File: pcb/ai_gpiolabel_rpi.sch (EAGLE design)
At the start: 3 parts

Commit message: updating
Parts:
- renumbered U$3 to LABEL
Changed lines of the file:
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@@
 <grid distance="50" unitdist="mil" unit="mil" style="lines" multiple="1" display="yes" altdistance="0.01" altunitdist="inch" altunit="inch"/>
 <layers>
-<layer number="1" name="Top" color="4" fill="1" visible="yes" active="no"/>
-<layer number="16" name="Bottom" color="1" fill="1" visible="yes" active="no"/>
-<layer number="17" name="Pads" color="2" fill="1" visible="yes" active="no"/>
-<layer number="18" name="Vias" color="2" fill="1" visible="yes" active="no"/>
-<layer number="19" name="Unrouted" color="6" fill="1" visible="yes" active="no"/>
-<layer number="20" name="Dimension" color="15" fill="1" visible="yes" active="no"/>
-<layer number="21" name="tPlace" color="7" fill="1" visible="yes" active="no"/>
-<layer number="22" name="bPlace" color="7" fill="1" visible="yes" active="no"/>
-<layer number="23" name="tOrigins" color="15" fill="1" visible="yes" active="no"/>
-<layer number="24" name="bOrigins" color="15" fill="1" visible="yes" active="no"/>
-<layer number="25" name="tNames" color="7" fill="1" visible="yes" active="no"/>
-<layer number="26" name="bNames" color="7" fill="1" visible="yes" active="no"/>
-<layer number="27" name="tValues" color="7" fill="1" visible="yes" active="no"/>
-<layer number="28" name="bValues" color="7" fill="1" visible="yes" active="no"/>
+<layer number="1" name="Top" color="4" fill="1" visible="no" active="no"/>
+<layer number="16" name="Bottom" color="1" fill="1" visible="no" active="no"/>
+<layer number="17" name="Pads" color="2" fill="1" visible="no" active="no"/>
+<layer number="18" name="Vias" color="2" fill="1" visible="no" active="no"/>
+<layer number="19" name="Unrouted" color="6" fill="1" visible="no" active="no"/>
+<layer number="20" name="Dimension" color="15" fill="1" visible="no" active="no"/>
+<layer number="21" name="tPlace" color="7" fill="1" visible="no" active="no"/>
+<layer number="22" name="bPlace" color="7" fill="1" visible="no" active="no"/>
+<layer number="23" name="tOrigins" color="15" fill="1" visible="no" active="no"/>
+<layer number="24" name="bOrigins" color="15" fill="1" visible="no" active="no"/>
+<layer number="25" name="tNames" color="7" fill="1" visible="no" active="no"/>
+<layer number="26" name="bNames" color="7" fill="1" visible="no" active="no"/>
+<layer number="27" name="tValues" color="7" fill="1" visible="no" active="no"/>
+<layer number="28" name="bValues" color="7" fill="1" visible="no" active="no"/>
 <layer number="29" name="tStop" color="7" fill="3" visible="no" active="no"/>
 <layer number="30" name="bStop" color="7" fill="6" visible="no" active="no"/>
@@
 <layer number="35" name="tGlue" color="7" fill="4" visible="no" active="no"/>
 <layer number="36" name="bGlue" color="7" fill="5" visible="no" active="no"/>
-<layer number="37" name="tTest" color="7" fill="1" visible="yes" active="no"/>
-<layer number="38" name="bTest" color="7" fill="1" visible="yes" active="no"/>
+<layer number="37" name="tTest" color="7" fill="1" visible="no" active="no"/>
+<layer number="38" name="bTest" color="7" fill="1" visible="no" active="no"/>
 <layer number="39" name="tKeepout" color="4" fill="11" visible="no" active="no"/>
 <layer number="40" name="bKeepout" color="1" fill="11" visible="no" active="no"/>
@@
 <layer number="44" name="Drills" color="7" fill="1" visible="no" active="no"/>
 <layer number="45" name="Holes" color="7" fill="1" visible="no" active="no"/>
-<layer number="46" name="Milling" color="3" fill="1" visible="yes" active="no"/>
-<layer number="47" name="Measures" color="7" fill="1" visible="yes" active="no"/>
-<layer number="48" name="Document" color="7" fill="1" visible="yes" active="no"/>
-<layer number="49" name="Reference" color="7" fill="1" visible="yes" active="no"/>
-<layer number="50" name="dxf" color="7" fill="1" visible="yes" active="no"/>
-<layer number="51" name="tDocu" color="7" fill="1" visible="yes" active="no"/>
-<layer number="52" name="bDocu" color="7" fill="1" visible="yes" active="no"/>
-<layer number="53" name="tGND_GNDA" color="7" fill="9" visible="yes" active="no"/>
-<layer number="54" name="bGND_GNDA" color="1" fill="9" visible="yes" active="no"/>
-<layer number="56" name="wert" color="7" fill="1" visible="yes" active="no"/>
-<layer number="57" name="tCAD" color="7" fill="1" visible="yes" active="no"/>
+<layer number="46" name="Milling" color="3" fill="1" visible="no" active="no"/>
+<layer number="47" name="Measures" color="7" fill="1" visible="no" active="no"/>
+<layer number="48" name="Document" color="7" fill="1" visible="no" active="no"/>
+<layer number="49" name="Reference" color="7" fill="1" visible="no" active="no"/>
+<layer number="50" name="dxf" color="7" fill="1" visible="no" active="no"/>
+<layer number="51" name="tDocu" color="7" fill="1" visible="no" active="no"/>
+<layer number="52" name="bDocu" color="7" fill="1" visible="no" active="no"/>
+<layer number="53" name="tGND_GNDA" color="7" fill="9" visible="no" active="no"/>
+<layer number="54" name="bGND_GNDA" color="1" fill="9" visible="no" active="no"/>
+<layer number="56" name="wert" color="7" fill="1" visible="no" active="no"/>
+<layer number="57" name="tCAD" color="7" fill="1" visible="no" active="no"/>
 <layer number="90" name="Modules" color="5" fill="1" visible="yes" active="yes"/>
 <layer number="91" name="Nets" color="2" fill="1" visible="yes" active="yes"/>
@@
 <layer number="97" name="Info" color="7" fill="1" visible="yes" active="yes"/>
 <layer number="98" name="Guide" color="6" fill="1" visible="yes" active="yes"/>
+<layer number="99" name="SpiceOrder" color="7" fill="1" visible="no" active="no"/>
 <layer number="100" name="Muster" color="7" fill="1" visible="no" active="no"/>
 <layer number="101" name="Patch_Top" color="12" fill="4" visible="no" active="yes"/>
@@
 </part>
 <part name="U$2" library="Ai_Miscellany" deviceset="AI-LOGO" device="XS"/>
-<part name="U$3" library="Ai_Connectors" deviceset="2X20-RPI" device="-NOFIRST" value="2X20-RPI-NOFIRST"/>
+<part name="LABEL" library="Ai_Connectors" deviceset="2X20-RPI" device="-NOFIRST" value="2X20-RPI-NOFIRST"/>
 <part name="U$4" library="Ai_Miscellany" deviceset="AI-LOGO" device="XS"/>
 </parts>
@@
 <instances>
 <instance part="FRAME1" gate="G$1" x="0" y="0"/>
-<instance part="FRAME1" gate="G$2" x="147.32" y="0"/>
-<instance part="U$2" gate="G$1" x="134.62" y="13.97"/>
-<instance part="U$3" gate="G$1" x="123.19" y="95.25"/>
-<instance part="U$4" gate="G$1" x="134.62" y="13.97"/>
+<instance part="FRAME1" gate="G$2" x="154.94" y="3.81"/>
+<instance part="U$2" gate="G$1" x="144.78" y="17.78"/>
+<instance part="LABEL" gate="G$1" x="123.19" y="95.25"/>
+<instance part="U$4" gate="G$1" x="144.78" y="16.51"/>
 </instances>
 <busses>

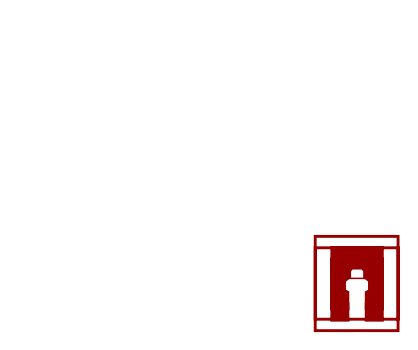
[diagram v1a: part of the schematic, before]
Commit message: Added README, LICENSE, and panelized
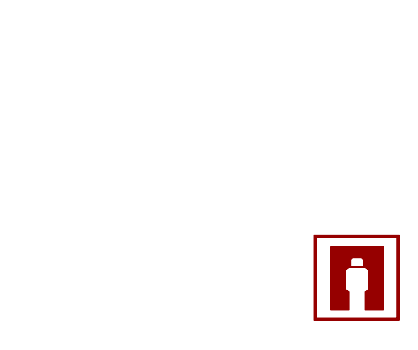
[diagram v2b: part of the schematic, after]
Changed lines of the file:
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@@
 <parts>
 <part name="FRAME1" library="Ai_Miscellany" deviceset="FRAME-LETTER" device="">
-<attribute name="AUTHOR" value="A.I. HARDWARE SITH LORDS"/>
 <attribute name="REV" value="1.0"/>
 </part>
@@
 <instance part="U$2" gate="G$1" x="144.78" y="17.78"/>
 <instance part="LABEL" gate="G$1" x="123.19" y="95.25"/>
-<instance part="U$4" gate="G$1" x="144.78" y="16.51"/>
+<instance part="U$4" gate="G$1" x="144.78" y="17.78"/>
 </instances>
 <busses>

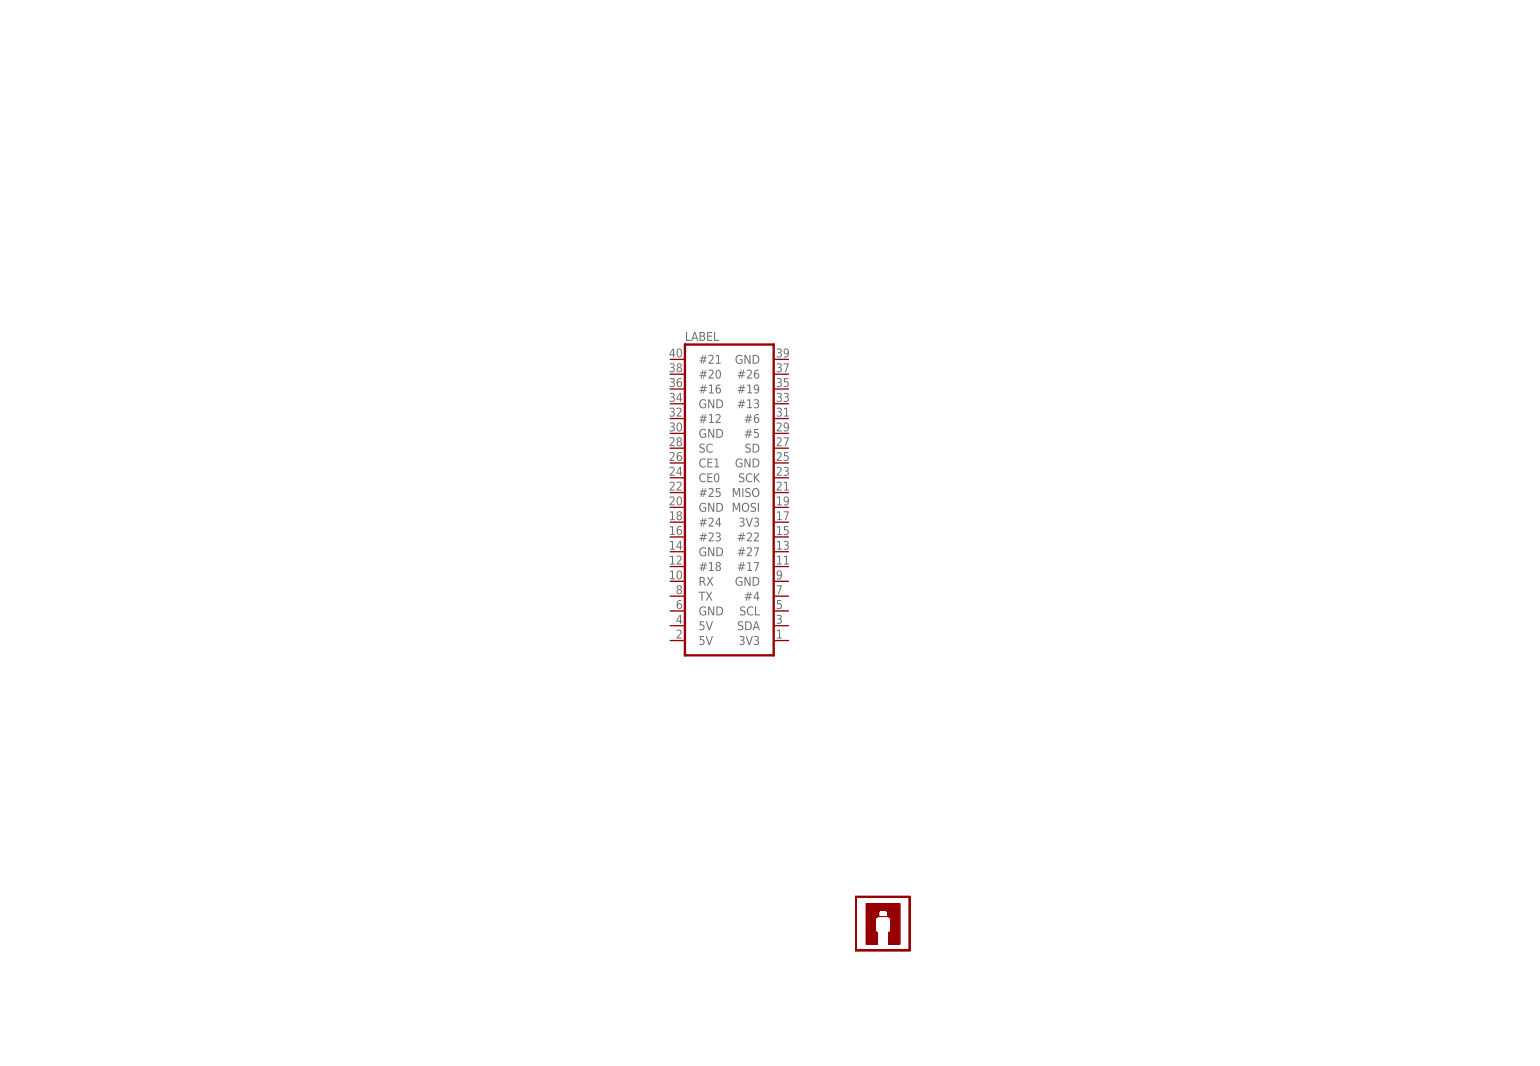
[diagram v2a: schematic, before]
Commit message: adding additional licensing information
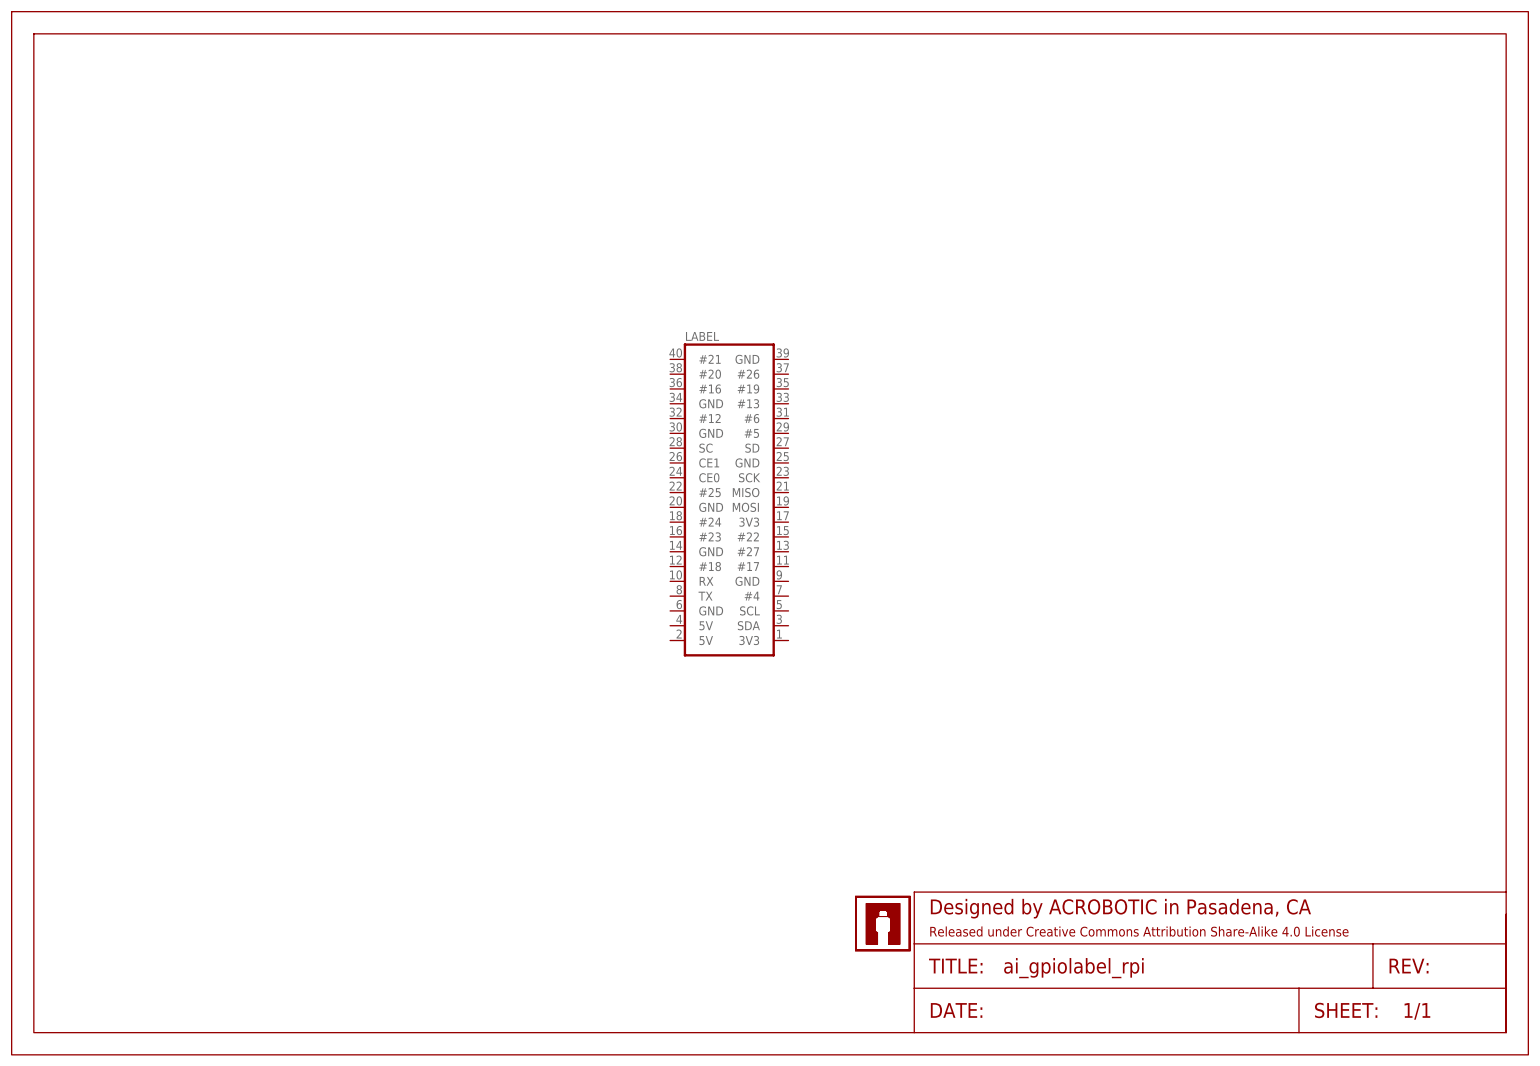
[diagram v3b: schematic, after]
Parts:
- added FRAME1: FRAME-LETTER, Ai_Miscellany:FRAME-LETTER
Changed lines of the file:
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@@
 <instances>
 <instance part="FRAME1" gate="G$1" x="0" y="0"/>
-<instance part="FRAME1" gate="G$2" x="154.94" y="3.81"/>
+<instance part="FRAME1" gate="G$2" x="154.94" y="3.81">
+<attribute name="REV" x="154.94" y="3.81" size="1.778" layer="96" display="off"/>
+</instance>
 <instance part="U$2" gate="G$1" x="144.78" y="17.78"/>
 <instance part="LABEL" gate="G$1" x="123.19" y="95.25"/>
@@
 </schematic>
 </drawing>
+<compatibility>
+<note version="6.3" minversion="6.2.2" severity="warning">
+Since Version 6.2.2 text objects can contain more than one line,
+which will not be processed correctly with this version.
+</note>
+</compatibility>
 </eagle>
